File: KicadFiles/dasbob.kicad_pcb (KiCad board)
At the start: 2 copper layers, 243.5 x 104.8 mm, 64 parts, among them J1 TRRS LEFT, J2 TRRS LEFT, SW1 SW_Push, SW10 SW_Push, SW11 SW_Push, SW12 SW_Push, SW13 SW_Push, SW14 SW_Push, SW15 SW_Push, SW16 SW_Push, SW17 SW_Push, SW18 SW_Push, SW19 SW_Push, SW2 SW_Push, SW20 SW_Push, SW21 SW_Push, SW22 SW_Push, SW23 SW_Push, SW24 SW_Push, SW25 SW_Push, SW26 SW_Push, SW27 SW_Push, SW28 SW_Push, SW29 SW_Push, SW3 SW_Push, SW30 SW_Push, SW31 SW_Push, SW32 SW_Push, SW33 SW_Push, SW34 SW_Push, SW35 SW_Push, SW36 SW_Push, SW4 SW_Push, SW5 SW_Push, SW6 SW_Push, SW7 SW_Push, SW8 SW_Push, SW9 SW_Push, U1 Elite-C RIGHT, U2 Elite-C LEFT, U3 OLED1, U4 OLED2

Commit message: v1.1
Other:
- board text added: "DASBOB REV 1.1"
- board text removed: "DASBOB REV 1"
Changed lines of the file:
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@@
   (gr_curve (pts (xy 149.767218 88.290471) (xy 149.964971 88.290471) (xy 150.125282 88.450781) (xy 150.125282 88.648534)) (layer "Edge.Cuts") (width 0.09))
   (gr_curve (pts (xy 193.409365 34.735277) (xy 193.409365 34.735277) (xy 157.884616 34.735277) (xy 157.884616 34.735277)) (layer "Edge.Cuts") (width 0.09))
-  (gr_text "DASBOB REV 1" (at 154.432565 65.823139 -90) (layer "B.SilkS")
+  (gr_text "DASBOB REV 1.1" (at 154.432565 65.823139 -90) (layer "B.SilkS")
     (effects (font (size 1 1) (thickness 0.25)) (justify mirror))
   )

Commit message: rev1.1
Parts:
- moved SW28 1.02 mm to (260.6, 72.9)
- moved SW33 1.02 mm to (257.6, 89.7)
- moved SW14 1.01 mm to (102.3, 76.1)
- moved SW15 1.01 mm to (120.3, 78.1)
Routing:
- net 14: track 63.5 -> 64.5 mm
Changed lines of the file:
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@@
   )
   (footprint "Beibob:Kailh_socket_PG1350_optional" (layer "F.Cu")
-    (at 120.325 79.09)
+    (at 120.325 78.08)
     (descr "Kailh \"Choc\" PG1350 keyswitch with optional socket mount")
     (tags "kailh,choc")
@@
   )
   (footprint "Beibob:Kailh_socket_PG1350_optional" (layer "F.Cu")
-    (at 260.372039 73.948304 -10)
+    (at 260.559535 72.94609 -10)
     (descr "Kailh \"Choc\" PG1350 keyswitch with optional socket mount")
     (tags "kailh,choc")
@@
   )
   (footprint "Beibob:Kailh_socket_PG1350_optional" (layer "F.Cu")
-    (at 257.412039 90.698304 -10)
+    (at 257.599535 89.69609 -10)
     (descr "Kailh \"Choc\" PG1350 keyswitch with optional socket mount")
     (tags "kailh,choc")
@@
   )
   (footprint "Beibob:Kailh_socket_PG1350_optional" (layer "F.Cu")
-    (at 102.315 77.12)
+    (at 102.32 76.11)
     (descr "Kailh \"Choc\" PG1350 keyswitch with optional socket mount")
     (tags "kailh,choc")
@@
   (segment (start 81.03 72.745) (end 81.03 64.17) (width 0.25) (layer "B.Cu") (net 15))
   (segment (start 84.305 76.02) (end 81.03 72.745) (width 0.25) (layer "B.Cu") (net 15))
-  (segment (start 120.97 86.55) (end 122.08 85.44) (width 0.25) (layer "F.Cu") (net 16))
-  (segment (start 102.315 83.02) (end 105.845 86.55) (width 0.25) (layer "F.Cu") (net 16))
-  (segment (start 127.91 82.75) (end 127.91 65.53) (width 0.25) (layer "F.Cu") (net 16))
+  (segment (start 105.84 86.55) (end 120.97 86.55) (width 0.25) (layer "F.Cu") (net 16))
   (segment (start 125.22 85.44) (end 127.91 82.75) (width 0.25) (layer "F.Cu") (net 16))
-  (segment (start 105.845 86.55) (end 120.97 86.55) (width 0.25) (layer "F.Cu") (net 16))
+  (segment (start 127.91 82.75) (end 127.91 65.53) (width 0.25) (layer "F.Cu") (net 16))
   (segment (start 127.91 65.53) (end 131.04 62.4) (width 0.25) (layer "F.Cu") (net 16))
+  (segment (start 102.32 82.01) (end 102.32 83.03) (width 0.25) (layer "F.Cu") (net 16))
   (segment (start 122.08 85.44) (end 125.22 85.44) (width 0.25) (layer "F.Cu") (net 16))
-  (segment (start 99.04 71.17) (end 99.04 79.745) (width 0.25) (layer "B.Cu") (net 16))
-  (segment (start 99.04 79.745) (end 102.315 83.02) (width 0.25) (layer "B.Cu") (net 16))
+  (segment (start 102.32 83.03) (end 105.84 86.55) (width 0.25) (layer "F.Cu") (net 16))
+  (segment (start 120.97 86.55) (end 122.08 85.44) (width 0.25) (layer "F.Cu") (net 16))
+  (segment (start 99.03 78.72) (end 102.32 82.01) (width 0.25) (layer "B.Cu") (net 16))
+  (segment (start 99.03 70.175) (end 99.03 78.72) (width 0.25) (layer "B.Cu") (net 16))
+  (segment (start 99.045 70.16) (end 99.03 70.175) (width 0.25) (layer "B.Cu") (net 16))
   (segment (start 125.02 84.99) (end 127.46 82.55) (width 0.25) (layer "F.Cu") (net 17))
   (segment (start 135.61 59.03) (end 145.76 59.03) (width 0.25) (layer "F.Cu") (net 17))
+  (segment (start 121.335 84.99) (end 120.325 83.98) (width 0.25) (layer "F.Cu") (net 17))
   (segment (start 129.91 61.39) (end 130.21 61.09) (width 0.25) (layer "F.Cu") (net 17))
-  (segment (start 125.02 84.99) (end 120.325 84.99) (width 0.25) (layer "F.Cu") (net 17))
   (segment (start 127.46 65.32) (end 129.91 62.87) (width 0.25) (layer "F.Cu") (net 17))
   (segment (start 129.91 62.87) (end 129.91 61.39) (width 0.25) (layer "F.Cu") (net 17))
@@
   (segment (start 130.21 61.09) (end 133.55 61.09) (width 0.25) (layer "F.Cu") (net 17))
   (segment (start 127.46 82.55) (end 127.46 65.32) (width 0.25) (layer "F.Cu") (net 17))
-  (segment (start 117.05 73.14) (end 117.05 81.715) (width 0.25) (layer "B.Cu") (net 17))
-  (segment (start 117.05 81.715) (end 120.325 84.99) (width 0.25) (layer "B.Cu") (net 17))
+  (segment (start 125.02 84.99) (end 121.335 84.99) (width 0.25) (layer "F.Cu") (net 17))
+  (segment (start 117.05 72.13) (end 117.05 80.705) (width 0.25) (layer "B.Cu") (net 17))
+  (segment (start 117.05 80.705) (end 120.325 83.98) (width 0.25) (layer "B.Cu") (net 17))
   (segment (start 122.84 87.24) (end 126 87.24) (width 0.25) (layer "F.Cu") (net 18))
   (segment (start 129.74 69.82) (end 130.65 68.91) (width 0.25) (layer "F.Cu") (net 18))
@@
   (segment (start 203.06 67.4) (end 215.07 67.4) (width 0.25) (layer "F.Cu") (net 32))
   (segment (start 177.69 66.95) (end 178.52 67.78) (width 0.25) (layer "F.Cu") (net 32))
+  (segment (start 250.27 66.11) (end 251.02 66.11) (width 0.25) (layer "F.Cu") (net 32))
   (segment (start 175.88 58.54) (end 176.99 59.65) (width 0.25) (layer "F.Cu") (net 32))
   (segment (start 178.52 67.78) (end 182.28 67.78) (width 0.25) (layer "F.Cu") (net 32))
-  (segment (start 256.66 77.071155) (end 259.347515 79.75867) (width 0.25) (layer "F.Cu") (net 32))
   (segment (start 177.69 63) (end 177.69 66.95) (width 0.25) (layer "F.Cu") (net 32))
+  (segment (start 231.46 66.11) (end 250.27 66.11) (width 0.25) (layer "F.Cu") (net 32))
   (segment (start 182.28 67.78) (end 184.36 69.86) (width 0.25) (layer "F.Cu") (net 32))
+  (segment (start 251.02 66.11) (end 257.335 72.425) (width 0.25) (layer "F.Cu") (net 32))
   (segment (start 160.81675 58.54) (end 175.88 58.54) (width 0.25) (layer "F.Cu") (net 32))
-  (segment (start 250.51 66.11) (end 256.66 72.26) (width 0.25) (layer "F.Cu") (net 32))
-  (segment (start 231.46 66.11) (end 250.51 66.11) (width 0.25) (layer "F.Cu") (net 32))
   (segment (start 215.07 67.4) (end 221.51 60.96) (width 0.25) (layer "F.Cu") (net 32))
   (segment (start 200.6 69.86) (end 203.06 67.4) (width 0.25) (layer "F.Cu") (net 32))
   (segment (start 176.99 62.3) (end 177.69 63) (width 0.25) (layer "F.Cu") (net 32))
+  (segment (start 250.27 66.11) (end 250.51 66.11) (width 0.25) (layer "F.Cu") (net 32))
   (segment (start 226.31 60.96) (end 231.46 66.11) (width 0.25) (layer "F.Cu") (net 32))
-  (segment (start 256.66 72.26) (end 256.66 77.071155) (width 0.25) (layer "F.Cu") (net 32))
   (segment (start 221.51 60.96) (end 226.31 60.96) (width 0.25) (layer "F.Cu") (net 32))
+  (segment (start 257.335 72.425) (end 257.335 76.556445) (width 0.25) (layer "F.Cu") (net 32))
   (segment (start 184.36 69.86) (end 200.6 69.86) (width 0.25) (layer "F.Cu") (net 32))
+  (segment (start 257.335 76.556445) (end 259.535011 78.756456) (width 0.25) (layer "F.Cu") (net 32))
   (segment (start 176.99 59.65) (end 176.99 62.3) (width 0.25) (layer "F.Cu") (net 32))
-  (segment (start 258.18 67.52) (end 258.18 78.591155) (width 0.25) (layer "B.Cu") (net 32))
-  (segment (start 258.18 78.591155) (end 259.347515 79.75867) (width 0.25) (layer "B.Cu") (net 32))
+  (segment (start 258.367496 77.588941) (end 259.535011 78.756456) (width 0.25) (layer "B.Cu") (net 32))
+  (segment (start 258.367496 66.517786) (end 258.367496 77.588941) (width 0.25) (layer "B.Cu") (net 32))
   (segment (start 176.53 62.48) (end 176.53 60.52) (width 0.25) (layer "F.Cu") (net 33))
   (segment (start 175.84675 59.83675) (end 174.76 59.83675) (width 0.25) (layer "F.Cu") (net 33))
@@
   (segment (start 170.9 66.1) (end 170.9 68.13) (width 0.25) (layer "F.Cu") (net 37))
   (segment (start 222.13 80.99) (end 237.25 80.99) (width 0.25) (layer "F.Cu") (net 37))
-  (segment (start 255.205 94.805) (end 256.387515 95.987515) (width 0.25) (layer "F.Cu") (net 37))
   (segment (start 177.04 69.55) (end 177.04 83.12) (width 0.25) (layer "F.Cu") (net 37))
   (segment (start 200.59 86.86) (end 201.61 85.84) (width 0.25) (layer "F.Cu") (net 37))
   (segment (start 239.31 83.05) (end 248.65 83.05) (width 0.25) (layer "F.Cu") (net 37))
   (segment (start 217.28 85.84) (end 222.13 80.99) (width 0.25) (layer "F.Cu") (net 37))
-  (segment (start 255.205 89.605) (end 255.205 94.805) (width 0.25) (layer "F.Cu") (net 37))
   (segment (start 171.65 68.88) (end 176.37 68.88) (width 0.25) (layer "F.Cu") (net 37))
+  (segment (start 254.6 89) (end 254.6 93.531445) (width 0.25) (layer "F.Cu") (net 37))
   (segment (start 201.61 85.84) (end 217.28 85.84) (width 0.25) (layer "F.Cu") (net 37))
   (segment (start 237.25 80.99) (end 239.31 83.05) (width 0.25) (layer "F.Cu") (net 37))
   (segment (start 179.15 85.23) (end 182.75 85.23) (width 0.25) (layer "F.Cu") (net 37))
   (segment (start 182.75 85.23) (end 184.38 86.86) (width 0.25) (layer "F.Cu") (net 37))
-  (segment (start 248.65 83.05) (end 255.205 89.605) (width 0.25) (layer "F.Cu") (net 37))
+  (segment (start 254.6 93.531445) (end 256.575011 95.506456) (width 0.25) (layer "F.Cu") (net 37))
   (segment (start 170.17 65.37) (end 170.9 66.1) (width 0.25) (layer "F.Cu") (net 37))
   (segment (start 170.9 68.13) (end 171.65 68.88) (width 0.25) (layer "F.Cu") (net 37))
   (segment (start 162.16 65.37) (end 170.17 65.37) (width 0.25) (layer "F.Cu") (net 37))
   (segment (start 177.04 83.12) (end 179.15 85.23) (width 0.25) (layer "F.Cu") (net 37))
+  (segment (start 248.65 83.05) (end 254.6 89) (width 0.25) (layer "F.Cu") (net 37))
   (segment (start 176.37 68.88) (end 177.04 69.55) (width 0.25) (layer "F.Cu") (net 37))
   (segment (start 184.38 86.86) (end 200.59 86.86) (width 0.25) (layer "F.Cu") (net 37))
-  (segment (start 255.22 95.341155) (end 256.387515 96.50867) (width 0.25) (layer "B.Cu") (net 37))
-  (segment (start 255.22 84.27) (end 255.22 95.341155) (width 0.25) (layer "B.Cu") (net 37))
+  (segment (start 255.407496 83.267786) (end 255.407496 94.338941) (width 0.25) (layer "B.Cu") (net 37))
+  (segment (start 255.407496 94.338941) (end 256.575011 95.506456) (width 0.25) (layer "B.Cu") (net 37))
   (segment (start 162.98 64.46) (end 162.25 63.73) (width 0.25) (layer "F.Cu") (net 38))
   (segment (start 188.25 108.54) (end 190.56 106.23) (width 0.25) (layer "F.Cu") (net 38))

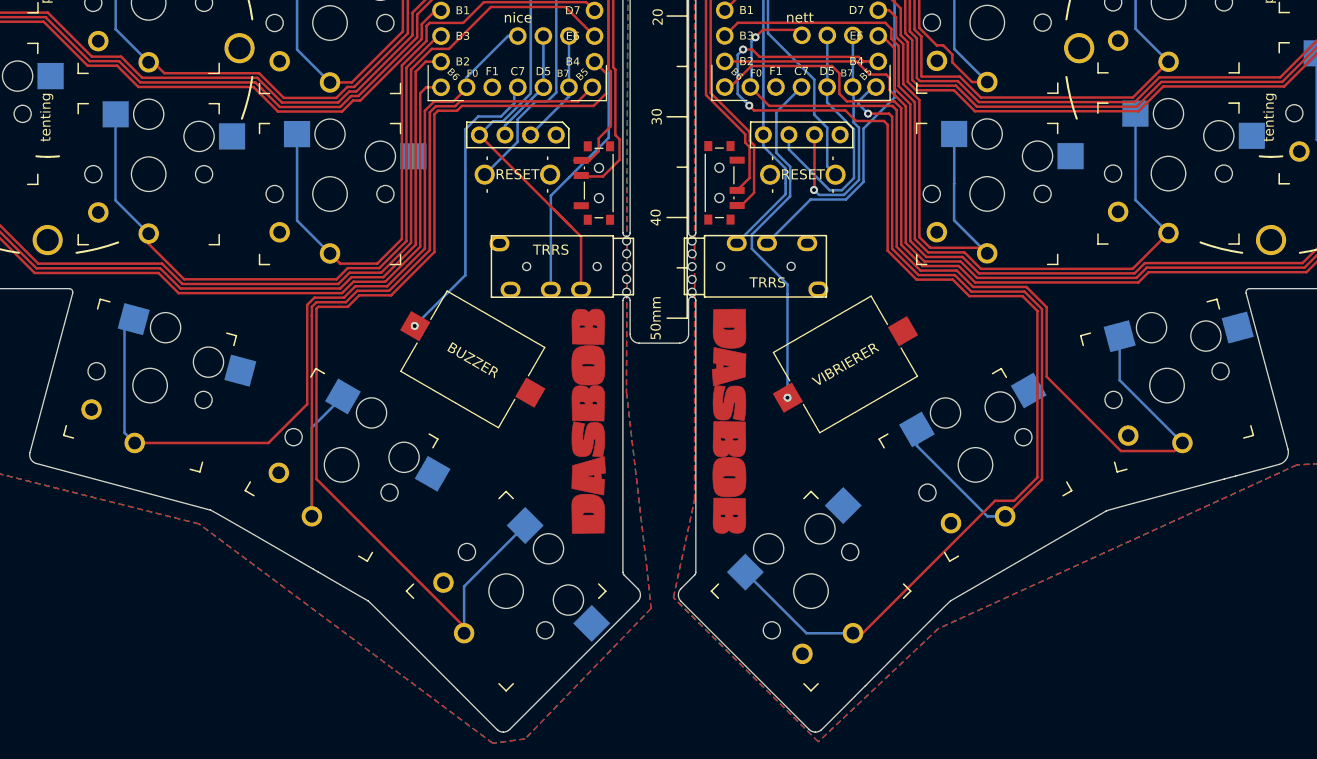
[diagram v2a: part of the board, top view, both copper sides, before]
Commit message: moved thumbs 1mm down
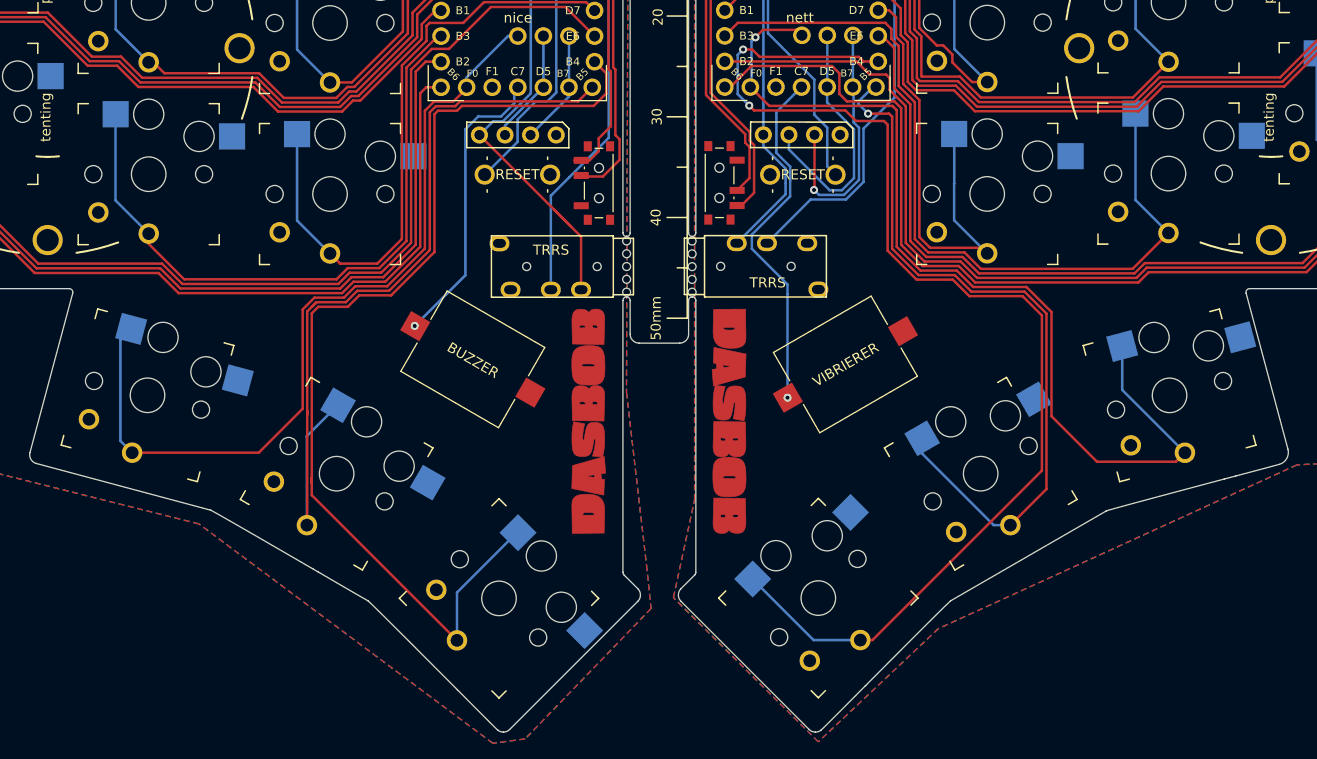
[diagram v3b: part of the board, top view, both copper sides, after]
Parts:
- moved SW35 1.02 mm to (184.9, 105.8)
- moved SW17 1.01 mm to (121.0, 105.8)
- moved SW18 1.01 mm to (137.1, 118.2)
- moved SW36 1.00 mm to (203.7, 98.1)
- moved SW34 1.00 mm to (168.8, 118.2)
- moved SW16 1.00 mm to (102.2, 98.1)
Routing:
- net 16a: track 93.7 -> 96.4 mm
- net 17a: track 72.0 -> 74.6 mm
- net 17: track 78.9 -> 81.0 mm
- net 16: track 80.9 -> 83.0 mm
- net 18: track 100.1 -> 102.2 mm
